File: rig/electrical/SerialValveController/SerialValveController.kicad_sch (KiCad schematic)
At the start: 21 parts, among them J1 Screw_Terminal_01x02, J17 Conn_01x05_Socket, J18 TST-105-01-X-D, J19 TST-105-01-X-D, J2 Screw_Terminal_01x02, U1 TPIC6595

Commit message: Serial Olfactometer improved design
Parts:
- R3, R4, R5, R6, R7: value R -> 33Ω
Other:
- company: (none) -> Ruta and Kronauer Labs, Rockefeller University
- title: (none) -> MultiBiOS Serial Valve Controller
- moved on the sheet: C2, C3, C4, CR1, CR2, D1, D2, H1, H2, J1, J17, J19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

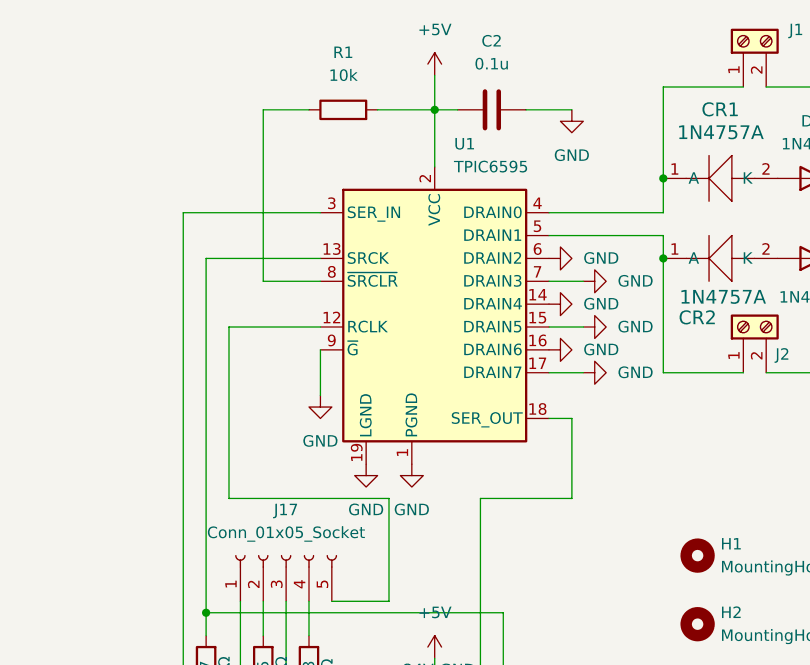
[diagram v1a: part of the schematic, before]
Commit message: valve updated
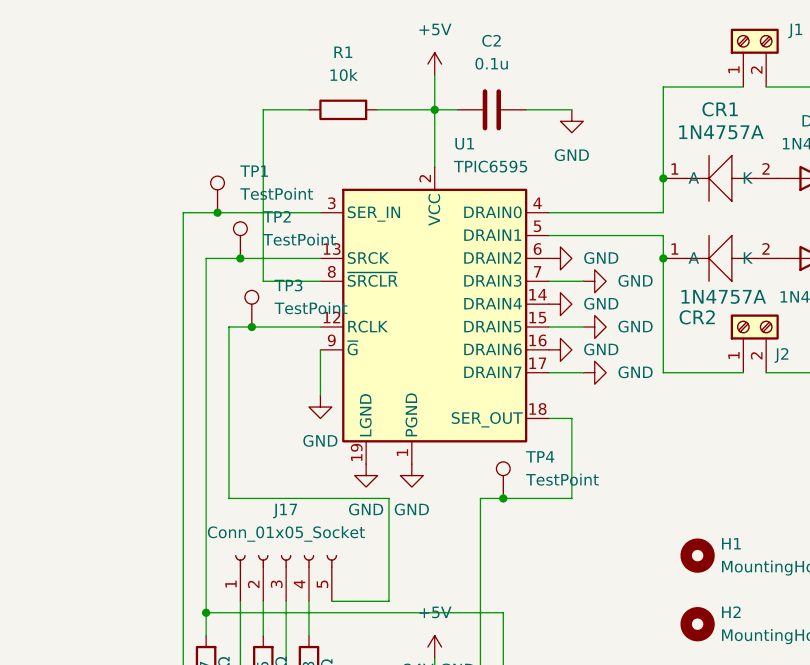
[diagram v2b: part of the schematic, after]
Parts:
- added TP1, TP2, TP3, TP4: TestPoint, TestPoint:TestPoint_Pad_2.0x2.0mm, symbol Connector:TestPoint
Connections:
- net at J19.01, R7.2, U1.13 (SRCK): now also TP2.1
- net at J17.5 (Pin_5), U1.12 (RCLK): now also TP3.1
- net at J19.03, U1.18 (SER_OUT): now also TP4.1
- net at J18.03, U1.3 (SER_IN): now also TP1.1
